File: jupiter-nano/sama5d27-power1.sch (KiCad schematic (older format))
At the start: 50 parts, among them U1 ATSAMA5D27C-LD1G-CU

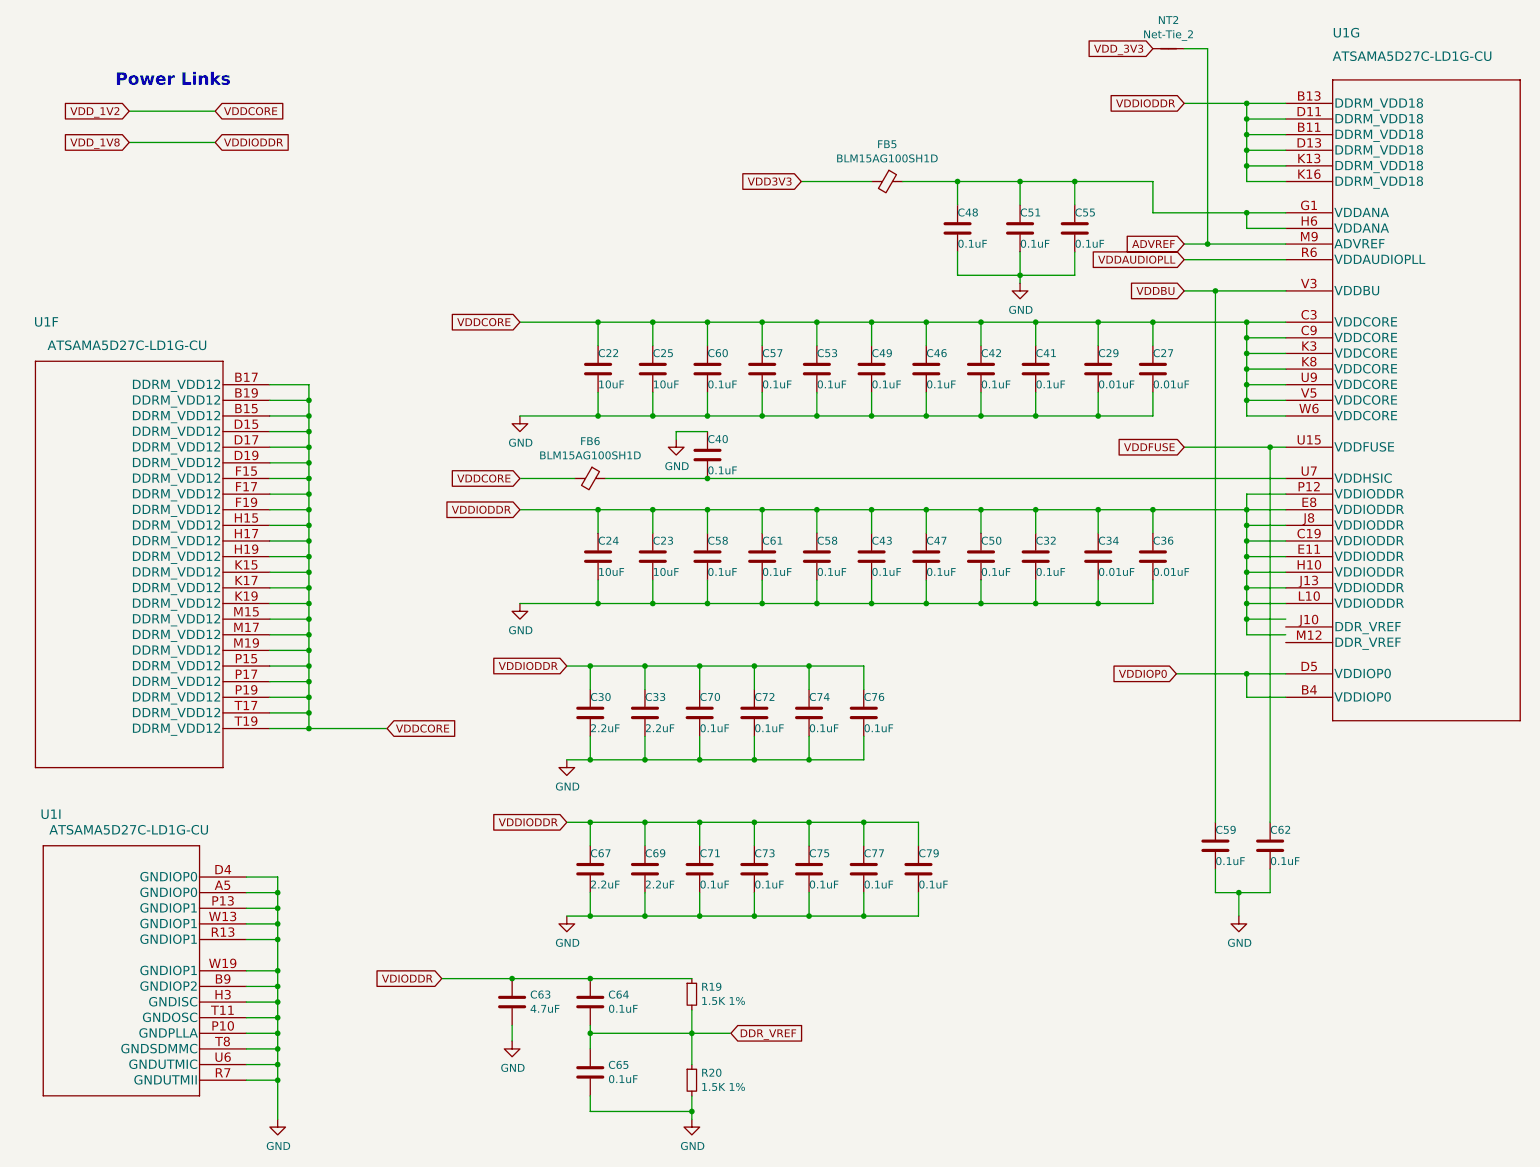
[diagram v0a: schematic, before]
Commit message: numerous ERC fixes
- still more to go
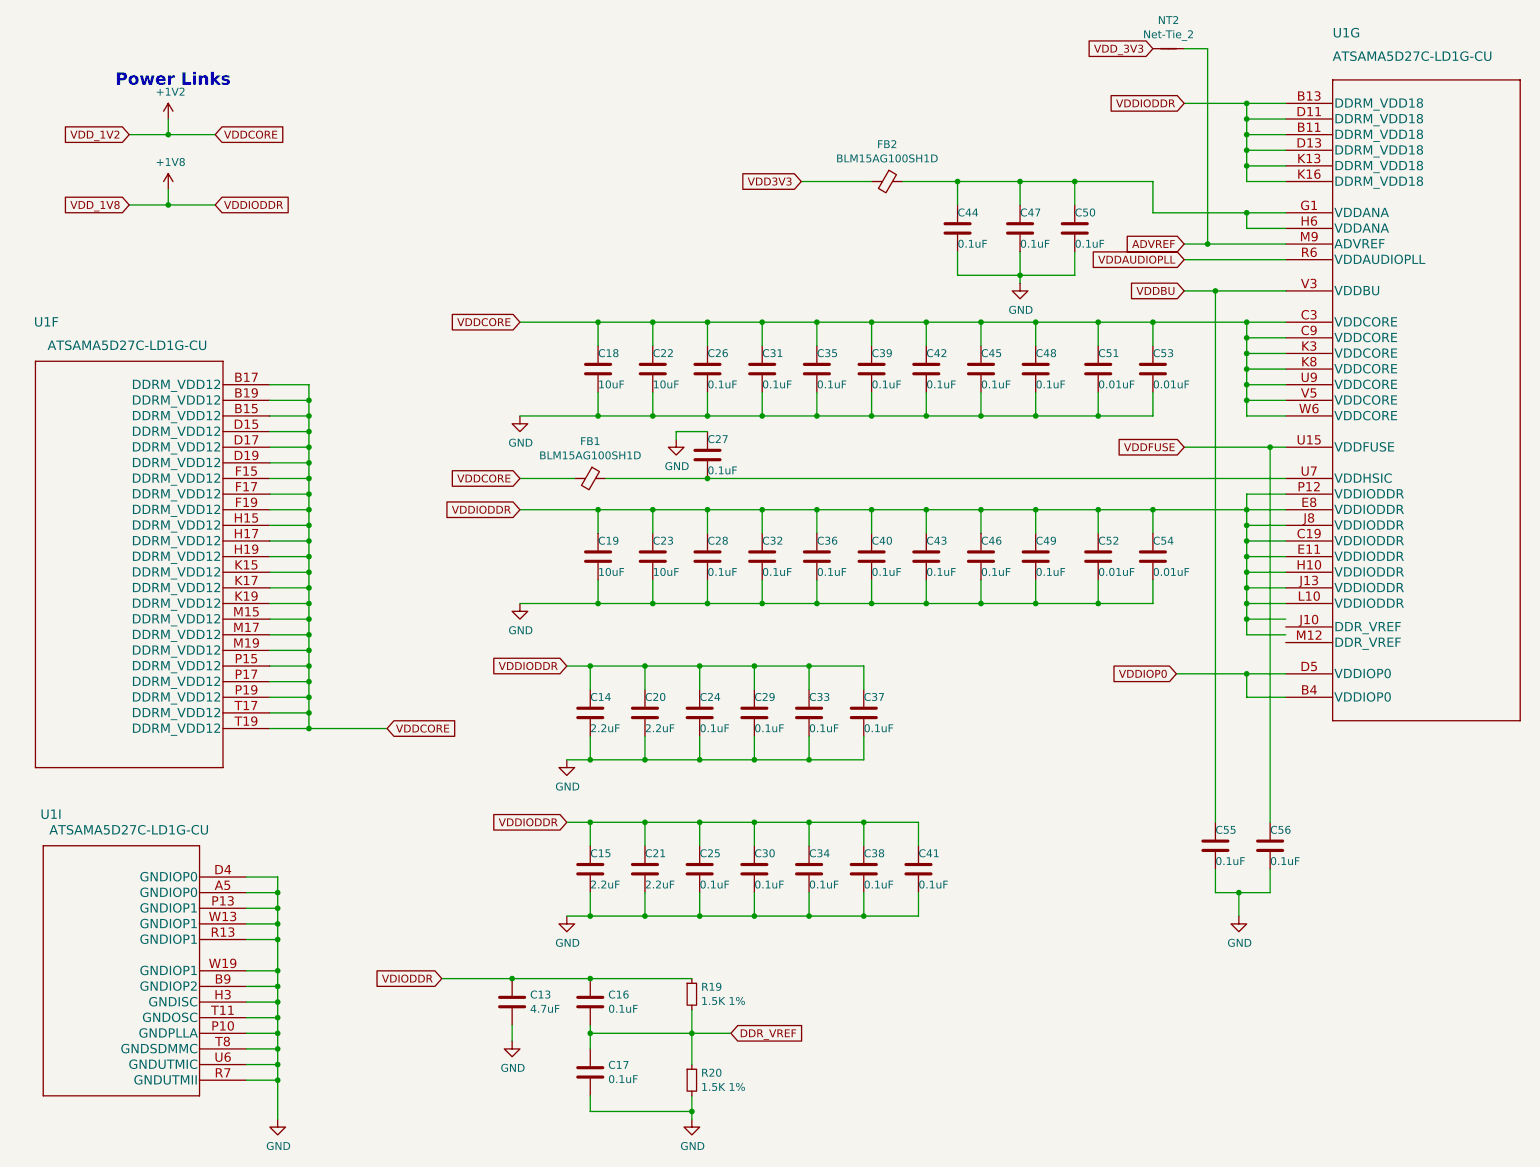
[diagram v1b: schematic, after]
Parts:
- renumbered C63 to C13, C30 to C14, C67 to C15, C64 to C16, C65 to C17, C22 to C18, C24 to C19, C33 to C20, C69 to C21, C25 to C22, C70 to C24, C71 to C25, C60 to C26, C40 to C27, C58 to C28, C72 to C29, C73 to C30, C57 to C31, C61 to C32, C74 to C33, C75 to C34, C53 to C35, C58 to C36, C76 to C37, C77 to C38, C49 to C39, C43 to C40, C79 to C41, C46 to C42, C47 to C43, C48 to C44, C42 to C45, C50 to C46, C51 to C47, C41 to C48, C32 to C49, C55 to C50, C29 to C51, C34 to C52, C27 to C53, C36 to C54, C59 to C55, C62 to C56, FB6 to FB1, FB5 to FB2
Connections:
- net VDDCORE renamed +1V2
- net VDDIODDR renamed +1V8

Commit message: added at24csw080 I2C EEPROM UUID chip
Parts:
- renumbered R19 to R22, R20 to R23
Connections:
- net VDD3V3 is gone; now on net VDDIOP0: FB2.2
- net VDD_3V3 is gone; now on net VDDIOP0: NT2.1
- net VDIODDR is gone; now on net VDDIODDR: C13.1, C16.1, R22.1
- net DDR_VREF: now also U1.J10 (DDR_VREF), U1.M12 (DDR_VREF)
- net GND: no longer U1.R7 (GNDUTMII)
- net +1V2 renamed VDDCORE
- net +1V8 renamed VDDIODDR
- net VDDFUSE renamed VDD_FUSE
- new net GNDUTMII: U1.R7 (GNDUTMII)
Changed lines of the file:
@@
 	1    0    0    -1
 $EndComp
-Text GLabel 1400 1250 0    50   Input ~ 0
+Text GLabel 1300 1250 0    50   Input ~ 0
 VDD_1V2
-Text GLabel 1400 1700 0    50   Input ~ 0
+Text GLabel 1300 1500 0    50   Input ~ 0
 VDD_1V8
-Text GLabel 1950 1250 2    50   Input ~ 0
+Text GLabel 1850 1250 2    50   Input ~ 0
 VDDCORE
-Text GLabel 1950 1700 2    50   Input ~ 0
+Text GLabel 1850 1500 2    50   Input ~ 0
 VDDIODDR
-Text Notes 2050 950  2    79   ~ 16
+Text Notes 1950 950  2    79   ~ 16
 Power Links
 Wire Wire Line
@@
 	2350 6000 2350 6100
 $Comp
-L power:GND #PWR033
+L power:GND #PWR034
 U 1 1 5FC7E204
 P 2350 7550
-F 0 "#PWR033" H 2350 7300 50  0001 C CNN
+F 0 "#PWR034" H 2350 7300 50  0001 C CNN
 F 1 "GND" H 2355 7377 50  0000 C CNN
 F 2 "" H 2350 7550 50  0001 C CNN
@@
 Connection ~ 2350 7200
 Wire Wire Line
-	2350 7200 2350 7300
-Wire Wire Line
 	2300 2850 2550 2850
 Wire Wire Line
@@
 Wire Wire Line
 	8800 4250 8550 4250
-Connection ~ 8550 4250
 Wire Wire Line
 	8550 4250 8550 4150
-Wire Wire Line
-	8800 4350 8550 4350
 Wire Wire Line
 	8800 1550 8550 1550
@@
 	7950 3050 7600 3050
 $Comp
-L power:GND #PWR035
+L power:GND #PWR036
 U 1 1 5FEF0D49
 P 3900 3050
-F 0 "#PWR035" H 3900 2800 50  0001 C CNN
+F 0 "#PWR036" H 3900 2800 50  0001 C CNN
 F 1 "GND" H 3905 2877 50  0000 C CNN
 F 2 "" H 3900 3050 50  0001 C CNN
@@
 	7100 2150 7100 2200
 $Comp
-L power:GND #PWR041
+L power:GND #PWR042
 U 1 1 6015BED8
 P 7100 2200
-F 0 "#PWR041" H 7100 1950 50  0001 C CNN
+F 0 "#PWR042" H 7100 1950 50  0001 C CNN
 F 1 "GND" H 7105 2027 50  0000 C CNN
 F 2 "" H 7100 2200 50  0001 C CNN
@@
 	6150 1550 5700 1550
 Text GLabel 5700 1550 0    50   Input ~ 0
-VDD3V3
+VDD_3V3
 Wire Wire Line
 	8550 1050 8150 1050
@@
 	6100 4650 5750 4650
 $Comp
-L power:GND #PWR037
+L power:GND #PWR038
 U 1 1 601D850A
 P 4200 5250
-F 0 "#PWR037" H 4200 5000 50  0001 C CNN
+F 0 "#PWR038" H 4200 5000 50  0001 C CNN
 F 1 "GND" H 4205 5077 50  0000 C CNN
 F 2 "" H 4200 5250 50  0001 C CNN
@@
 	6450 5650 6100 5650
 $Comp
-L power:GND #PWR038
+L power:GND #PWR039
 U 1 1 601FB1E3
 P 4200 6250
-F 0 "#PWR038" H 4200 6000 50  0001 C CNN
+F 0 "#PWR039" H 4200 6000 50  0001 C CNN
 F 1 "GND" H 4205 6077 50  0000 C CNN
 F 2 "" H 4200 6250 50  0001 C CNN
@@
 $EndComp
 $Comp
-L Device:R_Small R19
+L Device:R_Small R22
 U 1 1 603E4D1F
 P 5000 6750
-F 0 "R19" H 5059 6796 50  0000 L CNN
+F 0 "R22" H 5059 6796 50  0000 L CNN
 F 1 "1.5K 1%" H 5059 6705 50  0000 L CNN
 F 2 "" H 5000 6750 50  0001 C CNN
@@
 $EndComp
 $Comp
-L Device:R_Small R20
+L Device:R_Small R23
 U 1 1 603E60F3
 P 5000 7300
-F 0 "R20" H 5059 7346 50  0000 L CNN
+F 0 "R23" H 5059 7346 50  0000 L CNN
 F 1 "1.5K 1%" H 5059 7255 50  0000 L CNN
 F 2 "" H 5000 7300 50  0001 C CNN
@@
 DDR_VREF
 Text GLabel 3400 6650 0    50   Input ~ 0
-VDIODDR
+VDDIODDR
 Wire Wire Line
 	3400 6650 3850 6650
@@
 Connection ~ 5000 7500
 $Comp
-L power:GND #PWR040
+L power:GND #PWR041
 U 1 1 60495110
 P 5000 7550
-F 0 "#PWR040" H 5000 7300 50  0001 C CNN
+F 0 "#PWR041" H 5000 7300 50  0001 C CNN
 F 1 "GND" H 5005 7377 50  0000 C CNN
 F 2 "" H 5000 7550 50  0001 C CNN
@@
 	3850 6950 3850 7050
 $Comp
-L power:GND #PWR034
+L power:GND #PWR035
 U 1 1 604B01C3
 P 3850 7050
-F 0 "#PWR034" H 3850 6800 50  0001 C CNN
+F 0 "#PWR035" H 3850 6800 50  0001 C CNN
 F 1 "GND" H 3855 6877 50  0000 C CNN
 F 2 "" H 3850 7050 50  0001 C CNN
@@
 	7950 4250 7600 4250
 $Comp
-L power:GND #PWR036
+L power:GND #PWR037
 U 1 1 5F636B7A
 P 3900 4250
-F 0 "#PWR036" H 3900 4000 50  0001 C CNN
+F 0 "#PWR037" H 3900 4000 50  0001 C CNN
 F 1 "GND" H 3905 4077 50  0000 C CNN
 F 2 "" H 3900 4250 50  0001 C CNN
@@
 	8700 6100 8500 6100
 $Comp
-L power:GND #PWR042
+L power:GND #PWR043
 U 1 1 5F845541
 P 8500 6250
-F 0 "#PWR042" H 8500 6000 50  0001 C CNN
+F 0 "#PWR043" H 8500 6000 50  0001 C CNN
 F 1 "GND" H 8505 6077 50  0000 C CNN
 F 2 "" H 8500 6250 50  0001 C CNN
@@
 Connection ~ 8700 3250
 Text GLabel 8150 3250 0    50   Input ~ 0
-VDDFUSE
+VDD_FUSE
 Text GLabel 8150 2050 0    50   Input ~ 0
 VDDAUDIOPLL
@@
 	2350 6400 2350 6600
 Wire Wire Line
-	2150 7300 2350 7300
-Connection ~ 2350 7300
-Wire Wire Line
-	2350 7300 2350 7550
-Wire Wire Line
 	8800 3550 8550 3550
 Wire Wire Line
@@
 Wire Wire Line
 	8550 4850 8800 4850
-Wire Wire Line
-	8800 4450 8550 4450
-Wire Wire Line
-	8550 4250 8550 4350
-Connection ~ 8550 4350
-Wire Wire Line
-	8550 4350 8550 4450
 Text GLabel 8150 1950 0    50   Input ~ 0
 ADVREF
@@
 	4900 3150 4900 3200
 $Comp
-L power:GND #PWR039
+L power:GND #PWR040
 U 1 1 602286E4
 P 4900 3200
-F 0 "#PWR039" H 4900 2950 50  0001 C CNN
+F 0 "#PWR040" H 4900 2950 50  0001 C CNN
 F 1 "GND" H 4905 3027 50  0000 C CNN
 F 2 "" H 4900 3200 50  0001 C CNN
@@
 	8800 3450 5100 3450
 Connection ~ 5100 3450
-$Comp
-L power:+1V8 #PWR?
-U 1 1 5F61303C
-P 1650 1600
-F 0 "#PWR?" H 1650 1450 50  0001 C CNN
-F 1 "+1V8" H 1665 1773 50  0000 C CNN
-F 2 "" H 1650 1600 50  0001 C CNN
-F 3 "" H 1650 1600 50  0001 C CNN
-	1    1650 1600
-	1    0    0    -1
-$EndComp
-Wire Wire Line
-	1400 1700 1650 1700
-Wire Wire Line
-	1400 1250 1650 1250
-$Comp
-L power:+1V2 #PWR?
-U 1 1 5F62FC63
-P 1650 1150
-F 0 "#PWR?" H 1650 1000 50  0001 C CNN
-F 1 "+1V2" H 1665 1323 50  0000 C CNN
-F 2 "" H 1650 1150 50  0001 C CNN
-F 3 "" H 1650 1150 50  0001 C CNN
-	1    1650 1150
-	1    0    0    -1
-$EndComp
-Wire Wire Line
-	1650 1600 1650 1700
-Connection ~ 1650 1700
-Wire Wire Line
-	1650 1700 1950 1700
-Wire Wire Line
-	1650 1150 1650 1250
-Connection ~ 1650 1250
-Wire Wire Line
-	1650 1250 1950 1250
+Wire Wire Line
+	2350 7200 2350 7550
+Wire Wire Line
+	2150 7300 2600 7300
+Text GLabel 2600 7300 2    50   Input ~ 0
+GNDUTMII
+Wire Wire Line
+	8800 4400 8550 4400
+Wire Wire Line
+	8550 4400 8550 4500
+Wire Wire Line
+	8550 4500 8800 4500
+Wire Wire Line
+	8550 4400 8100 4400
+Connection ~ 8550 4400
+Text GLabel 8100 4400 0    50   Input ~ 0
+DDR_VREF
+Text GLabel 1300 1750 0    50   Input ~ 0
+VDD_3V3
+Text GLabel 1850 1750 2    50   Input ~ 0
+VDDIOP0
+Wire Wire Line
+	1300 1750 1850 1750
+Wire Wire Line
+	1300 1500 1850 1500
+Wire Wire Line
+	1300 1250 1850 1250
 $EndSCHEMATC
